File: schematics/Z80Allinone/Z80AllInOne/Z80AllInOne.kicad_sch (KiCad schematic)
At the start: 27 parts, among them J10 CF Card IDE, J4 TTL SERIAL, J8 TRGS/TOS, J9 9VDC, U13 7400, U14 74LS138, U15 74LS139, U24 Z80-CTC, U27 74HC00, U29 L7805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

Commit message: Latest modifications of All-in-one PCB
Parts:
- removed J9: 9VDC, TerminalBlock:TerminalBlock_bornier-2_P5.08mm, symbol Connector:Screw_Terminal_01x02
- added C53: 100uF, Capacitor_THT:CP_Radial_D8.0mm_P3.80mm, symbol Device:C_Polarized
- added C54: 10uF, Capacitor_THT:CP_Radial_D8.0mm_P3.80mm, symbol Device:C_Polarized
- added D12: DIODE, Diode_THT:D_A-405_P7.62mm_Horizontal, symbol pspice:DIODE
- C44: value 47uF -> 0.1uF
- C45: value 4.7uF -> 0.1uF
- R42: footprint Resistor_THT:R_Axial_DIN0207_L6.3mm_D2.5mm_P7.62mm_Horizontal -> Resistor_THT:R_Axial_DIN0207_L6.3mm_D2.5mm_P10.16mm_Horizontal
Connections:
- net GND: now also JP5.2, JP5.3, C53.2, C54.2; no longer JP5.1
- net VCC: now also C54.1, D12.1 (K)
- net at C44.1, D3.2 (A), U29.1 (IN): now also C53.1, D12.2 (A)
- net at D3.1 (K): now also JP5.1; no longer JP5.3
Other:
- moved on the sheet: D3, JP5

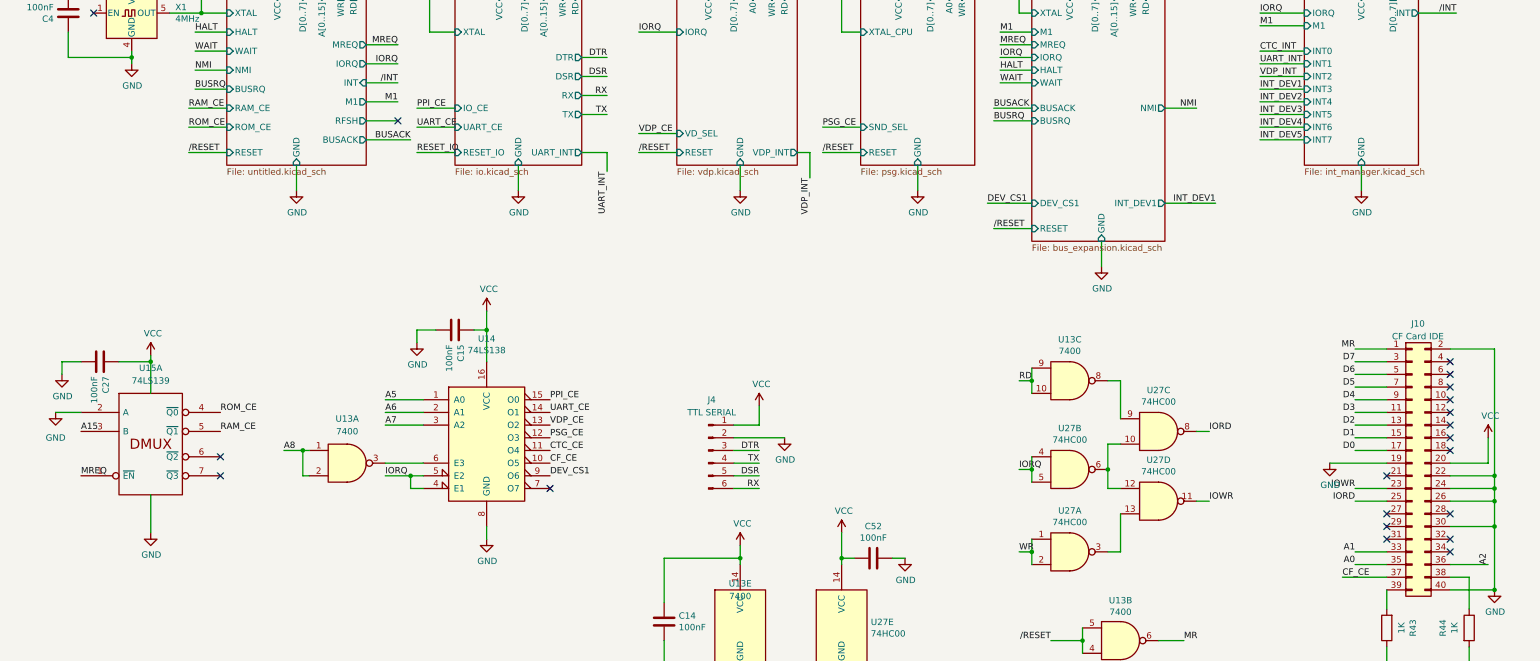
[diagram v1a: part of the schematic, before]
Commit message: Latest changes for adapt source to support Z80AllInOne adding some macros and latest schematic improvements
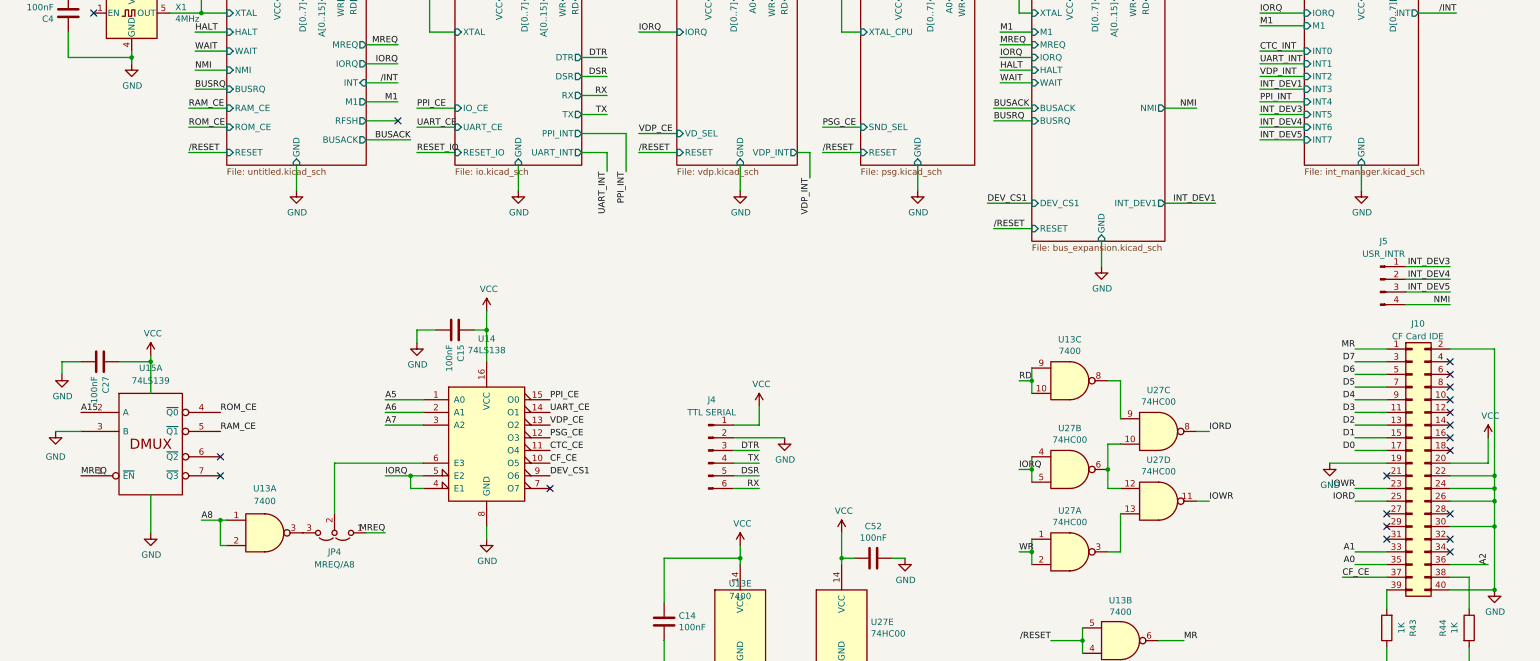
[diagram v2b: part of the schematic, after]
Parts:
- added J5: USR_INTR, Connector_PinHeader_2.54mm:PinHeader_1x04_P2.54mm_Vertical, symbol Connector:Conn_01x04_Male
- added JP4: MREQ/A8, Connector_PinHeader_2.54mm:PinHeader_1x03_P2.54mm_Vertical, symbol Jumper:Jumper_3_Open
- R11: footprint Resistor_THT:R_Axial_DIN0207_L6.3mm_D2.5mm_P7.62mm_Horizontal -> Resistor_THT:R_Axial_DIN0207_L6.3mm_D2.5mm_P10.16mm_Horizontal
- U29: footprint Package_TO_SOT_THT:TO-126-3_Horizontal_TabDown -> Package_TO_SOT_THT:TO-220-3_Horizontal_TabDown
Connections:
- net A15: now also U15.2 (A); no longer U15.3 (B)
- net GND: now also U15.3 (B); no longer U15.2 (A)
- net INT_DEV3: now also J5.1 (Pin_1)
- net INT_DEV4: now also J5.2 (Pin_2)
- net INT_DEV5: now also J5.3 (Pin_3)
- net MREQ: now also JP4.1 (A)
- net NMI: now also J5.4 (Pin_4)
- net at U14.6 (E3): now also JP4.2 (C); no longer U13.3
- new net: JP4.3 (B), U13.3
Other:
- sheet IO ports: added PPI_INT; removed none
- moved on the sheet: U13A

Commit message: Latest code and schematic updates. Changed IDE connector to 2.54mm IDE connector
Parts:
- J10: footprint Connector_PinHeader_2.00mm:PinHeader_2x20_P2.00mm_Vertical -> Connector_IDC:IDC-Header_2x20_P2.54mm_Vertical
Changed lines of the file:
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@@
       (effects (font (size 1.27 1.27)) (justify right))
     )
-    (property "Footprint" "Connector_PinHeader_2.00mm:PinHeader_2x20_P2.00mm_Vertical" (id 2) (at 293.37 185.42 0)
+    (property "Footprint" "Connector_IDC:IDC-Header_2x20_P2.54mm_Vertical" (id 2) (at 293.37 185.42 0)
       (effects (font (size 1.27 1.27)) hide)
     )
@@
     )
     (path "/b7886d78-4480-4e86-b304-8d6c50c98eaa"
-      (reference "J10") (unit 1) (value "CF Card IDE") (footprint "Connector_PinHeader_2.00mm:PinHeader_2x20_P2.00mm_Vertical")
+      (reference "J10") (unit 1) (value "CF Card IDE") (footprint "Connector_IDC:IDC-Header_2x20_P2.54mm_Vertical")
     )
     (path "/8d56bc60-b04c-4adc-bf64-8e46195cb167/f174a3a7-91a1-458f-8bb4-a754507a43eb"

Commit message: Latest changes and replace CTC for 8253 PIT
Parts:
- removed J8: TRGS/TOS, Connector_PinHeader_2.54mm:PinHeader_1x07_P2.54mm_Vertical, symbol Connector:Conn_01x07_Male
- removed R42: 10K, Resistor_THT:R_Axial_DIN0207_L6.3mm_D2.5mm_P10.16mm_Horizontal, symbol Device:R
- removed unit 2 of U13
- removed unit 3 of U13
- removed U24: Z80-CTC, Package_DIP:DIP-28_W15.24mm_LongPads, symbol ZILOG:Z80-CTC
- removed U27: 74HC00, Package_DIP:DIP-14_W7.62mm, symbol 74xx:74HC00
- added C37: C, Capacitor_THT:C_Disc_D7.0mm_W2.5mm_P5.00mm, symbol Device:C
- added J8: TMR_GS, Connector_PinHeader_2.54mm:PinHeader_1x04_P2.54mm_Vertical, symbol Connector:Conn_01x04_Male
- added unit 4 of U13
- added unit 3 of U13
- added unit 2 of U13
- added U17: 74HC04, Package_DIP:DIP-14_W7.62mm_Socket_LongPads, symbol 74xx:74HC04
- added U24: 8253, Package_DIP:DIP-24_W15.24mm, symbol Timer:8253
- added U25: 74LS32, Package_DIP:DIP-14_W7.62mm_LongPads, symbol 74xx:74LS32
- added U30: 74LS74, Package_DIP:DIP-14_W7.62mm_LongPads, symbol 74xx:74LS74
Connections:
- net A0: now also U24.19 (A0)
- net A1: now also U24.20 (A1)
- net CTC_CE: now also U24.21 (~{CS})
- net CTC_INT: now also U17.12
- net D0: now also U24.8 (D0)
- net D1: now also U24.7 (D1)
- net D2: now also U24.6 (D2)
- net D3: now also U24.5 (D3)
- net D4: now also U24.4 (D4)
- net D5: now also U24.3 (D5)
- net D6: now also U24.2 (D6)
- net D7: now also U24.1 (D7)
- net GND: now also C52.2, C37.1, U24.12 (GND), U25.7 (GND), U30.7 (GND); no longer C52.1
- net IORD: now also U13.6
- net IORQ: now also U25.12, U25.9
- net IOWR: now also U13.8
- net MR: now also U13.11
- net RD: now also U25.10
- net VCC: now also C52.1, C37.2, U24.11 (G0), U24.24 (VCC), U25.14 (VCC), U30.1 (~{R}), U30.10 (~{S}), U30.13 (~{R}), U30.14 (VCC), U30.4 (~{S}); no longer C52.2
- net WR: now also U25.13
- net XTAL: now also U30.3 (C)
- net /RESET: now also U13.12, U13.13
- new net: U24.9 (CLK0), U30.11 (C), U30.5 (Q)
- new net: U30.12 (D), U30.8 (~{Q})
- new net: U24.15 (CLK1), U30.9 (Q)
- new net: U17.13, U24.10 (OUT0)
- new net: J8.4 (Pin_4), U24.13 (OUT1), U24.18 (CLK2)
- new net: J8.3 (Pin_3), U24.14 (G1)
- new net: J8.2 (Pin_2), U24.16 (G2)
- new net: J8.1 (Pin_1), U24.17 (OUT2)
- new net: U30.2 (D), U30.6 (~{Q})
- new net /IOR: U13.4, U13.5, U24.22 (~{RD}), U25.8
- new net /IOW: U13.10, U13.9, U24.23 (~{WR}), U25.11
- no-connect marks 21 -> 20
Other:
- sheet SOUND ports: added /NMI; removed none
- moved on the sheet: C14, C39, U13E

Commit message: Created new macro for LOADCNT PIT counter reset and removed old CTC routines that not used.
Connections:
- net XTAL_DIV2: now reaches U24.9 (CLK0), U30.11 (C), U30.5 (Q)
- net XTAL_DIV4: now reaches U24.15 (CLK1), U30.9 (Q)
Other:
- sheet SOUND ports: added XTAL_DIV2; removed XTAL_CPU
- moved on the sheet: U17F
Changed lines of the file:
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@@
   (junction (at 309.88 198.12) (diameter 0) (color 0 0 0 0)
   )
-  (junction (at 179.07 80.01) (diameter 0) (color 0 0 0 0)
-  )
   (junction (at 309.88 193.04) (diameter 0) (color 0 0 0 0)
   )
@@
   (junction (at 60.96 52.07) (diameter 0) (color 0 0 0 0)
   )
+  (junction (at 381 69.85) (diameter 0) (color 0 0 0 0)
+  )
   (junction (at 83.82 52.07) (diameter 0) (color 0 0 0 0)
   )
@@
   (junction (at 31.75 43.18) (diameter 0) (color 0 0 0 0)
   )
+  (junction (at 401.32 69.85) (diameter 0) (color 0 0 0 0)
+  )
   (junction (at 36.83 86.36) (diameter 0) (color 0 0 0 0)
   )
@@
     (stroke (width 0) (type default) (color 0 0 0 0))
   )
-  (wire (pts (xy 179.07 80.01) (xy 214.63 80.01))
-    (stroke (width 0) (type default) (color 0 0 0 0))
-  )
   (wire (pts (xy 403.86 74.93) (xy 403.86 59.69))
     (stroke (width 0) (type default) (color 0 0 0 0))
@@
     (stroke (width 0) (type default) (color 0 0 0 0))
   )
-  (wire (pts (xy 179.07 80.01) (xy 179.07 99.06))
-    (stroke (width 0) (type default) (color 0 0 0 0))
-  )
   (wire (pts (xy 27.94 245.11) (xy 27.94 236.22))
     (stroke (width 0) (type default) (color 0 0 0 0))
@@
     (stroke (width 0) (type default) (color 0 0 0 0))
   )
+  (wire (pts (xy 351.79 93.98) (xy 351.79 96.52))
+    (stroke (width 0) (type default) (color 0 0 0 0))
+  )
   (wire (pts (xy 165.1 40.64) (xy 172.72 40.64))
     (stroke (width 0) (type default) (color 0 0 0 0))
@@
     (stroke (width 0) (type default) (color 0 0 0 0))
   )
-  (wire (pts (xy 351.79 93.98) (xy 367.03 93.98))
+  (wire (pts (xy 351.79 96.52) (xy 365.76 96.52))
     (stroke (width 0) (type default) (color 0 0 0 0))
   )
@@
     (stroke (width 0) (type default) (color 0 0 0 0))
   )
+  (wire (pts (xy 401.32 53.34) (xy 401.32 69.85))
+    (stroke (width 0) (type default) (color 0 0 0 0))
+  )
   (wire (pts (xy 95.25 24.13) (xy 95.25 38.1))
     (stroke (width 0) (type default) (color 0 0 0 0))
@@
     (stroke (width 0) (type default) (color 0 0 0 0))
   )
-  (wire (pts (xy 351.79 91.44) (xy 354.33 91.44))
+  (wire (pts (xy 351.79 91.44) (xy 384.81 91.44))
     (stroke (width 0) (type default) (color 0 0 0 0))
   )
@@
     (stroke (width 0) (type default) (color 0 0 0 0))
   )
-  (wire (pts (xy 96.52 80.01) (xy 179.07 80.01))
+  (wire (pts (xy 96.52 80.01) (xy 214.63 80.01))
     (stroke (width 0) (type default) (color 0 0 0 0))
   )
@@
     (stroke (width 0) (type default) (color 0 0 0 0))
   )
-  (wire (pts (xy 391.16 93.98) (xy 382.27 93.98))
+  (wire (pts (xy 391.16 96.52) (xy 381 96.52))
     (stroke (width 0) (type default) (color 0 0 0 0))
   )
@@
     (stroke (width 0) (type default) (color 0 0 0 0))
   )
-  (wire (pts (xy 179.07 99.06) (xy 182.88 99.06))
+  (wire (pts (xy 172.72 99.06) (xy 182.88 99.06))
     (stroke (width 0) (type default) (color 0 0 0 0))
   )
@@
     (stroke (width 0) (type default) (color 0 0 0 0))
   )
+  (wire (pts (xy 381 53.34) (xy 381 69.85))
+    (stroke (width 0) (type default) (color 0 0 0 0))
+  )
   (wire (pts (xy 57.15 246.38) (xy 57.15 237.49))
     (stroke (width 0) (type default) (color 0 0 0 0))
@@
     (effects (font (size 1.27 1.27)) (justify left bottom))
   )
+  (label "XTAL_DIV2" (at 172.72 99.06 0)
+    (effects (font (size 1.27 1.27)) (justify left bottom))
+  )
   (label "NMI" (at 250.19 114.3 180)
     (effects (font (size 1.27 1.27)) (justify right bottom))
@@
     (effects (font (size 1.27 1.27)) (justify left bottom))
   )
+  (label "XTAL_DIV4" (at 401.32 53.34 0)
+    (effects (font (size 1.27 1.27)) (justify left bottom))
+  )
   (label "BUSRQ" (at 49.53 110.49 0)
     (effects (font (size 1.27 1.27)) (justify left bottom))
@@
     (effects (font (size 1.27 1.27)) (justify left bottom))
   )
+  (label "XTAL_DIV2" (at 381 53.34 0)
+    (effects (font (size 1.27 1.27)) (justify left bottom))
+  )
   (label "D1" (at 281.94 180.34 180)
     (effects (font (size 1.27 1.27)) (justify right bottom))
@@
     (effects (font (size 1.27 1.27)) (justify right bottom))
   )
-  (label "CTC_INT" (at 391.16 93.98 180)
+  (label "CTC_INT" (at 391.16 96.52 180)
     (effects (font (size 1.27 1.27)) (justify right bottom))
   )
@@
     (pin "1")
   )
-  (symbol (lib_id "74xx:74HC04") (at 374.65 93.98 0) (unit 6)
+  (symbol (lib_id "74xx:74HC04") (at 373.38 96.52 0) (unit 6)
     (in_bom yes) (on_board yes)
-    (property "Reference" "U17" (id 0) (at 374.65 85.9282 0))
-    (property "Value" "74HC04" (id 1) (at 374.65 88.2396 0))
-    (property "Footprint" "Package_DIP:DIP-14_W7.62mm_Socket_LongPads" (id 2) (at 374.65 93.98 0)
+    (property "Reference" "U17" (id 0) (at 373.38 88.4682 0))
+    (property "Value" "74HC04" (id 1) (at 373.38 90.7796 0))
+    (property "Footprint" "Package_DIP:DIP-14_W7.62mm_Socket_LongPads" (id 2) (at 373.38 96.52 0)
       (effects (font (size 1.27 1.27)) hide)
     )
-    (property "Datasheet" "https://assets.nexperia.com/documents/data-sheet/74HC_HCT04.pdf" (id 3) (at 374.65 93.98 0)
+    (property "Datasheet" "https://assets.nexperia.com/documents/data-sheet/74HC_HCT04.pdf" (id 3) (at 373.38 96.52 0)
       (effects (font (size 1.27 1.27)) hide)
     )
@@
     (pin "7")
   )
-  (symbol (lib_id "power:VCC") (at 354.33 91.44 0) (unit 1)
+  (symbol (lib_id "power:VCC") (at 384.81 91.44 0) (unit 1)
     (in_bom yes) (on_board yes)
-    (property "Reference" "#PWR?" (id 0) (at 354.33 95.25 0)
+    (property "Reference" "#PWR0117" (id 0) (at 384.81 95.25 0)
       (effects (font (size 1.27 1.27)) hide)
     )
-    (property "Value" "VCC" (id 1) (at 354.7618 87.0458 0))
-    (property "Footprint" "" (id 2) (at 354.33 91.44 0)
+    (property "Value" "VCC" (id 1) (at 385.2418 87.0458 0))
+    (property "Footprint" "" (id 2) (at 384.81 91.44 0)
       (effects (font (size 1.27 1.27)) hide)
     )
-    (property "Datasheet" "" (id 3) (at 354.33 91.44 0)
+    (property "Datasheet" "" (id 3) (at 384.81 91.44 0)
       (effects (font (size 1.27 1.27)) hide)
     )
@@
       (effects (font (size 1.27 1.27)) (justify left))
     )
-    (pin "XTAL_CPU" input (at 182.88 99.06 180)
+    (pin "XTAL_DIV2" input (at 182.88 99.06 180)
       (effects (font (size 1.27 1.27)) (justify left))
     )
@@
       (reference "#PWR0116") (unit 1) (value "GND") (footprint "")
     )
+    (path "/f857da00-e963-4fe0-94b3-2c4b20c796e9"
+      (reference "#PWR0117") (unit 1) (value "VCC") (footprint "")
+    )
     (path "/c7b178f0-ea1a-4493-9f33-8d72ff2748ef/05641d68-cf6f-48e1-920a-7fd74222a8fa"
       (reference "#PWR0119") (unit 1) (value "GND") (footprint "")
@@
       (reference "#PWR0182") (unit 1) (value "VCC") (footprint "")
     )
-    (path "/f857da00-e963-4fe0-94b3-2c4b20c796e9"
-      (reference "#PWR?") (unit 1) (value "VCC") (footprint "")
-    )
     (path "/c7b178f0-ea1a-4493-9f33-8d72ff2748ef/8ca60f47-d255-4edd-9da7-5935bc1f59b5"
